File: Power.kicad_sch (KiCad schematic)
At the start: 76 parts, among them U1 TPS546D24ARVFR, U3 TPSM861253RDXR, U4 TPS546D24ARVFR, U5 L78L05_SOT89

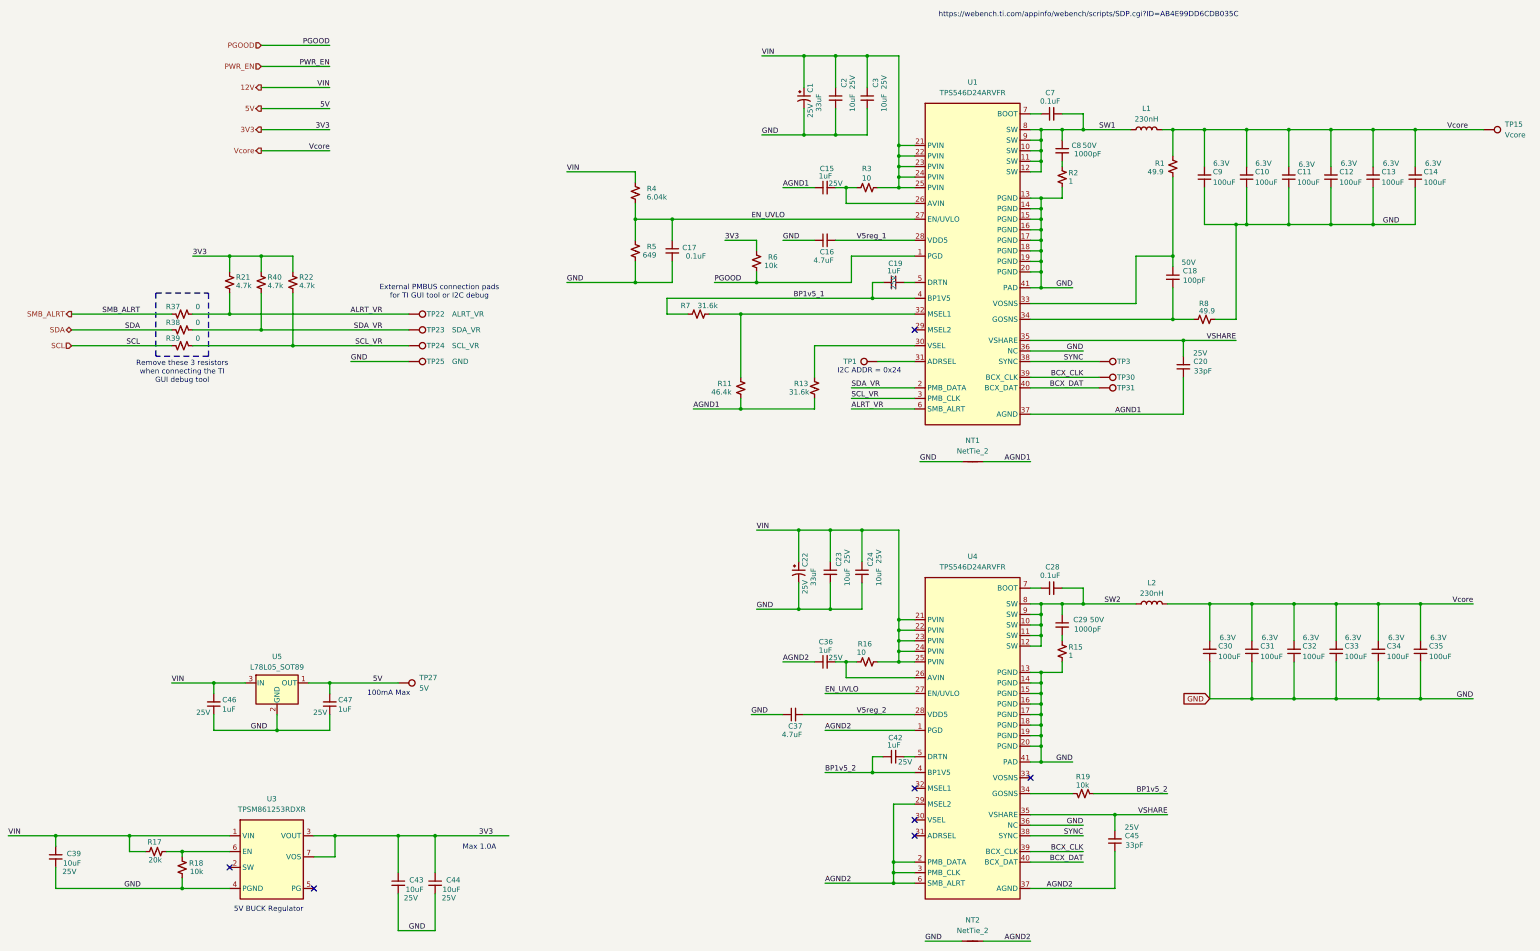
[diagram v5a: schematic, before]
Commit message: switched to single phase TPS546D24 and put the ASICs in series.
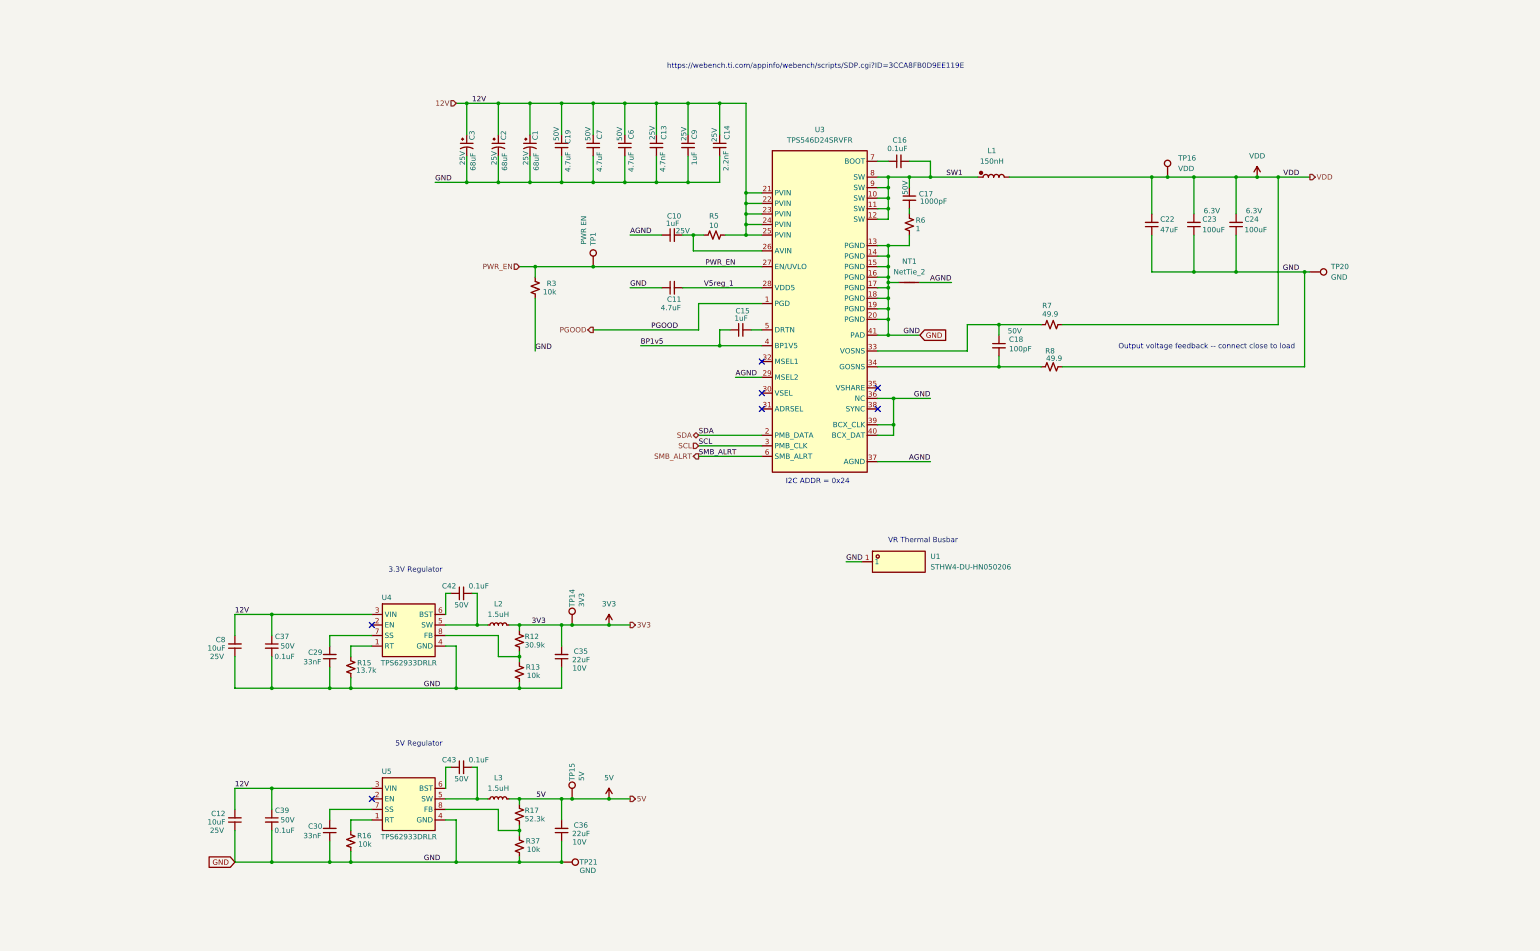
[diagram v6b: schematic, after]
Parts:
- removed C2, C3, C44: 10uF, Capacitor_SMD:C_0603_1608Metric, symbol Device:C_Small
- removed C20, C45: 33pF, Capacitor_SMD:C_0402_1005Metric, symbol Device:C_Small
- removed C22: 33uF, Capacitor_Tantalum_SMD:CP_EIA-7343-31_Kemet-D, symbol Device:C_Polarized_Small_US
- removed C28: 0.1uF, Capacitor_SMD:C_0402_1005Metric, symbol Device:C_Small
- removed C31, C32, C33, C34: 100uF, Capacitor_SMD:C_1206_3216Metric, symbol Device:C_Small
- removed C46, C47: 1uF, Capacitor_SMD:C_0402_1005Metric, symbol Device:C_Small
- removed L1, L2: 230nH, bitaxe:FP1107R1, symbol Device:L
- removed NT1, NT2: NetTie_2, bitaxe:NetTie-2_SMD_Pad0.2mmx1mm, symbol Device:NetTie_2
- removed R1: 49.9, Resistor_SMD:R_0402_1005Metric, symbol Device:R_Small_US
- removed R11: 46.4k, Resistor_SMD:R_0402_1005Metric, symbol Device:R_Small_US
- removed R18, R19: 10k, Resistor_SMD:R_0402_1005Metric, symbol Device:R_Small_US
- removed R2: 1, Resistor_SMD:R_0805_2012Metric, symbol Device:R_Small_US
- removed R21, R22, R40: 4.7k, Resistor_SMD:R_0402_1005Metric, symbol Device:R_Small_US
- removed R38, R39: 0, Resistor_SMD:R_0402_1005Metric, symbol Device:R_Small_US
- removed R4: 6.04k, Resistor_SMD:R_0402_1005Metric, symbol Device:R_Small_US
- removed TP22: ALRT_VR, TestPoint:TestPoint_Pad_D1.0mm, symbol Connector:TestPoint
- removed TP23: SDA_VR, TestPoint:TestPoint_Pad_D1.0mm, symbol Connector:TestPoint
- removed TP24: SCL_VR, TestPoint:TestPoint_Pad_D1.0mm, symbol Connector:TestPoint
- removed TP25: GND, TestPoint:TestPoint_Pad_D1.0mm, symbol Connector:TestPoint
- removed TP27: 5V, TestPoint:TestPoint_Pad_D1.5mm, symbol Connector:TestPoint
- removed TP3, TP30: BCX_CLK, TestPoint:TestPoint_Pad_D1.0mm, symbol Connector:TestPoint
- removed TP31: BCX_DAT, TestPoint:TestPoint_Pad_D1.0mm, symbol Connector:TestPoint
- removed U1, U4: TPS546D24ARVFR, bitaxe:LQFN40-CLIP, symbol bitaxe:TPS546D24
- removed U3: TPSM861253RDXR, bitaxe:TPSM863257RDX, symbol bitaxe:TPSM861253RDXR
- removed U5: L78L05_SOT89, Package_TO_SOT_SMD:SOT-89-3, symbol Regulator_Linear:L78L05_SOT89
- added C2, C3: 68uF, Capacitor_SMD:CP_Elec_5x5.8, symbol Device:C_Polarized_Small_US
- added C22: 47uF, Capacitor_SMD:C_0805_2012Metric, symbol Device:C_Small
- added C6: 4.7uF, Capacitor_SMD:C_1206_3216Metric, symbol Device:C_Small
- added L1: 150nH, symbol bitaxe:L-polarized
- added L2, L3: 1.5uH, bitaxe:IND-SMD_L2.0-W1.6, symbol Device:L_Small
- added NT1: NetTie_2, bitaxe:NetTie-2_SMD_Pad0.2mmx1mm, symbol bitaxe:NetTie_2
- added R12: 30.9k, Resistor_SMD:R_0402_1005Metric, symbol Device:R_Small_US
- added TP14: 3V3, bitaxe:TestPoint_Pad_D1.0mm, symbol Connector:TestPoint
- added TP16: VDD, bitaxe:TestPoint_Pad_D1.0mm, symbol Connector:TestPoint
- added TP20, TP21: GND, bitaxe:TestPoint_Pad_D1.0mm, symbol Connector:TestPoint
- added U1: STHW4-DU-HN050206, bitaxeProto:PAD-SMD_L5.0-W2.0_STHW4-DU-HN050206, symbol bitaxe:STHW4-DU-HN050206
- added U3: TPS546D24SRVFR, bitaxe:LQFN40-CLIP, symbol bitaxe:TPS546D24
- added U4, U5: TPS62933DRLR, bitaxe:SOT-583-8_L2.1-W1.2-P0.50-LS1.6-BR, symbol bitaxe:TPS62933DRLR
- C1: value 33uF -> 68uF; footprint Capacitor_Tantalum_SMD:CP_EIA-7343-31_Kemet-D -> Capacitor_SMD:CP_Elec_5x5.8; DK 399-3882-1-ND -> 493-16429-1-ND; PARTNO T495D336K025ATE300 -> UCM1E680MCL1GS
- C10, C9: value 100uF -> 1uF; footprint Capacitor_SMD:C_1206_3216Metric -> Capacitor_SMD:C_0603_1608Metric; DK 1276-1782-1-ND -> 1276-1184-1-ND; PARTNO CL31A107MQHNNNE -> CL10B105KA8NNNC; Voltage 6.3V -> 25V
- C11: value 100uF -> 4.7uF; footprint Capacitor_SMD:C_1206_3216Metric -> Capacitor_SMD:C_0402_1005Metric; DK 1276-1782-1-ND -> 490-14306-1-ND; PARTNO CL31A107MQHNNNE -> GRM155R61A475MEAAD; Voltage 6.3V -> (none)
- C12: value 100uF -> 10uF; footprint Capacitor_SMD:C_1206_3216Metric -> Capacitor_SMD:C_0603_1608Metric; DK 1276-1782-1-ND -> 490-18214-1-ND; LCSC (none) -> C15850; PARTNO CL31A107MQHNNNE -> GRM188R61E106KA73D; Voltage 6.3V -> 25V
- C13: value 100uF -> 4.7nF; footprint Capacitor_SMD:C_1206_3216Metric -> Capacitor_SMD:C_0402_1005Metric; DK 1276-1782-1-ND -> 490-1309-1-ND; PARTNO CL31A107MQHNNNE -> GRM155R71E472KA01D; Voltage 6.3V -> 25V
- C14: value 100uF -> 2.2nF; footprint Capacitor_SMD:C_1206_3216Metric -> Capacitor_SMD:C_0402_1005Metric; DK 1276-1782-1-ND -> 490-8257-1-ND; PARTNO CL31A107MQHNNNE -> GRM155R61H222KA01D; Voltage 6.3V -> 25V
- C15: DK 587-2984-1-ND -> 587-5514-1-ND; LCSC (none) -> C52923; PARTNO TMK107B7105KA-T -> EMK105BJ105MV-F; Voltage 25V -> (none)
- C16, C37: value 4.7uF -> 0.1uF; DK 490-14306-1-ND -> 490-10700-1-ND; LCSC (none) -> C77020; PARTNO GRM155R61A475MEAAD -> GRM155R71H104KE14D; Voltage (none) -> 50V
- C17: value 0.1uF -> 1000pF; footprint Capacitor_SMD:C_0402_1005Metric -> Capacitor_SMD:C_0805_2012Metric; DK 478-KGM05AR71C104KHCT-ND -> 311-1127-1-ND; PARTNO KGM05AR71C104KH -> CC0805KRX7R9BB102; Voltage (none) -> 50V
- C19: value 1uF -> 4.7uF; footprint Capacitor_SMD:C_0402_1005Metric -> Capacitor_SMD:C_1206_3216Metric; DK 587-2984-1-ND -> 490-6521-1-ND; PARTNO TMK107B7105KA-T -> GRM31CR71H475KA12L; Voltage 25V -> 50V
- C23, C24: value 10uF -> 100uF; footprint Capacitor_SMD:C_0603_1608Metric -> Capacitor_SMD:C_1210_3225Metric; DK 490-18214-1-ND -> 490-6533-1-ND; PARTNO GRM188R61E106KA73D -> GRM32EC80J107ME20L; Voltage 25V -> 6.3V
- C29: value 1000pF -> 33nF; footprint Capacitor_SMD:C_0805_2012Metric -> Capacitor_SMD:C_0402_1005Metric; DK 311-1127-1-ND -> 13-CC0402KRX7R9BB333CT-ND; LCSC (none) -> C106862; PARTNO CC0805KRX7R9BB102 -> CC0402KRX7R9BB333; Voltage 50V -> (none)
- C30: value 100uF -> 33nF; footprint Capacitor_SMD:C_1206_3216Metric -> Capacitor_SMD:C_0402_1005Metric; DK 1276-1782-1-ND -> 13-CC0402KRX7R9BB333CT-ND; LCSC (none) -> C106862; PARTNO CL31A107MQHNNNE -> CC0402KRX7R9BB333; Voltage 6.3V -> (none)
- C35: value 100uF -> 22uF; footprint Capacitor_SMD:C_1206_3216Metric -> Capacitor_SMD:C_0805_2012Metric; DK 1276-1782-1-ND -> 1276-2910-1-ND; LCSC (none) -> C45783; PARTNO CL31A107MQHNNNE -> CL21A226MPQNNNE; Voltage 6.3V -> 10V
- C36: value 1uF -> 22uF; footprint Capacitor_SMD:C_0402_1005Metric -> Capacitor_SMD:C_0805_2012Metric; DK 587-2984-1-ND -> 1276-2910-1-ND; LCSC (none) -> C45783; PARTNO TMK107B7105KA-T -> CL21A226MPQNNNE; Voltage 25V -> 10V
- C39: value 10uF -> 0.1uF; footprint Capacitor_SMD:C_0603_1608Metric -> Capacitor_SMD:C_0402_1005Metric; DK 490-18214-1-ND -> 490-10700-1-ND; LCSC (none) -> C77020; PARTNO GRM188R61E106KA73D -> GRM155R71H104KE14D; Voltage 25V -> 50V
- C42: value 1uF -> 0.1uF; DK 587-2984-1-ND -> 490-10700-1-ND; LCSC (none) -> C77020; Manufacturer (none) -> Murata Electronics; PARTNO TMK107B7105KA-T -> GRM155R71H104KE14D; Voltage 25V -> 50V
- C43: value 10uF -> 0.1uF; footprint Capacitor_SMD:C_0603_1608Metric -> Capacitor_SMD:C_0402_1005Metric; DK 490-18214-1-ND -> 490-10700-1-ND; LCSC (none) -> C77020; Manufacturer (none) -> Murata Electronics; PARTNO GRM188R61E106KA73D -> GRM155R71H104KE14D; Voltage 25V -> 50V
- C7: value 0.1uF -> 4.7uF; footprint Capacitor_SMD:C_0402_1005Metric -> Capacitor_SMD:C_1206_3216Metric; DK 478-KGM05AR71C104KHCT-ND -> 490-6521-1-ND; PARTNO KGM05AR71C104KH -> GRM31CR71H475KA12L; Voltage (none) -> 50V
- C8: value 1000pF -> 10uF; footprint Capacitor_SMD:C_0805_2012Metric -> Capacitor_SMD:C_0603_1608Metric; DK 311-1127-1-ND -> 490-18214-1-ND; LCSC (none) -> C15850; PARTNO CC0805KRX7R9BB102 -> GRM188R61E106KA73D; Voltage 50V -> 25V
- R13: value 31.6k -> 10k; DK YAG3115CT-ND -> 311-10KJRCT-ND; LCSC (none) -> C25744; PARTNO RC0402FR-0731K6L -> RC0402JR-0710KL
- R15: value 1 -> 13.7k; footprint Resistor_SMD:R_0805_2012Metric -> Resistor_SMD:R_0402_1005Metric; DK RHM1KTR-ND -> 311-13.7KLRCT-ND; LCSC (none) -> C274888; PARTNO ESR10EZPJ1R0 -> RC0402FR-0713K7L
- R16, R3: value 10 -> 10k; DK 311-10.0LRCT-ND -> 311-10KJRCT-ND; LCSC (none) -> C25744; PARTNO RC0402FR-0710RL -> RC0402JR-0710KL
- R17: value 20k -> 52.3k; DK 311-20.0KLRCT-ND -> YAG3179CT-ND; PARTNO RC0402FR-0720KL -> RC0402FR-0752K3L
- R37: value 0 -> 10k; DK 311-0.0JRCT-ND -> 311-10KJRCT-ND; LCSC (none) -> C25744; PARTNO RC0402JR-070RL -> RC0402JR-0710KL
- R5: value 649 -> 10; DK YAG3206CT-ND -> 311-10.0LRCT-ND; PARTNO RC0402FR-07649RL -> RC0402FR-0710RL
- R6: value 10k -> 1; footprint Resistor_SMD:R_0402_1005Metric -> Resistor_SMD:R_0805_2012Metric; DK 311-10KJRCT-ND -> RHM1KCT-ND; PARTNO RC0402JR-0710KL -> ESR10EZPJ1R0
- R7: value 31.6k -> 49.9; DK YAG3115CT-ND -> 311-49.9LRCT-ND; PARTNO RC0402FR-0731K6L -> RC0402FR-0749R9L
- TP1: value TestPoint -> PWR EN; footprint TestPoint:TestPoint_Pad_D1.0mm -> bitaxe:TestPoint_Pad_D1.0mm
- TP15: value Vcore -> 5V; footprint TestPoint:TestPoint_Pad_D1.5mm -> bitaxe:TestPoint_Pad_D1.0mm
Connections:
- net AGND2 is gone; now on net GND: C36.1
- net ALRT_VR is gone; now on an unnamed net: R37.2
- net SW2 is gone; now on net GND: C29.1
- net V5reg_2 is gone; now on net GND: C37.2
- net 12V: now also C12.2, C13.1, C14.1, C19.1, C37.1, C7.1, C8.2, C9.1, R5.1, C2.1, C3.1, C6.1, U3.21 (PVIN), U3.22 (PVIN), U3.23 (PVIN), U3.24 (PVIN), U3.25 (PVIN), U4.3 (VIN), U5.3 (VIN); no longer C23.1, C24.1, R16.1, R17.2, R3.1
- net 3V3: now also C35.2, L2.2, R12.2, TP14.1; no longer C43.1, R6.2
- net 5V: now also C36.2, R17.2, TP15.1, L3.2
- net GND: now also C13.2, C14.2, C19.2, C23.1, C24.1, C7.2, C8.1, C9.2, R13.1, R15.1, R16.1, R3.1, R37.1, R6.2, C2.2, C22.1, C3.2, C6.2, NT1.1, TP20.1, TP21.1, U1.1, U3.13 (PGND), U3.14 (PGND), U3.15 (PGND), U3.16 (PGND), U3.17 (PGND), U3.18 (PGND), U3.19 (PGND), U3.20 (PGND), U3.36 (NC), U3.39 (BCX_CLK), U3.40 (BCX_DAT), U3.41 (PAD), U4.4 (GND), U5.4 (GND); no longer C10.1, C13.1, C14.1, C16.1, C17.2, C23.2, C24.2, C37.1, C43.2, C9.1, R15.2, R5.1
- net PGOOD: now also U3.1 (PGD); no longer R6.1
- net PWR_EN: now also R3.2, TP1.1, U3.27 (EN/UVLO)
- net SCL: now also U3.3 (PMB_CLK)
- net SDA: now also U3.2 (PMB_DATA)
- net SMB_ALRT: now also U3.6 (SMB_ALRT); no longer R37.1
- net SW1: now also C16.2, C17.1, L1.1, U3.10 (SW), U3.11 (SW), U3.12 (SW), U3.8 (SW), U3.9 (SW); no longer C7.2, C8.1
- net V5reg_1: now also C11.2, U3.28 (VDD5); no longer C16.2
- net at C18.2, R8.1: now also U3.34 (GOSNS)
- net VDD: now reaches R7.1
- net VDD: now also C23.2, C24.2, C22.2, L1.2, TP16.1
- net at R17.1: now also U5.8 (FB)
- net at C18.1: now also R7.2, U3.33 (VOSNS)
- net at C29.2: now also U4.7 (SS); no longer R15.1
- net at C15.2: now also U3.5 (DRTN); no longer R3.2
- net at R13.2: now also R12.1, U4.8 (FB)
- net at R16.2: now also U5.1 (RT); no longer C36.2
- net at C42.2: now also L2.1, U4.5 (SW)
- net AGND1 renamed BP1v5
- net BP1v5: now also U3.4 (BP1V5); no longer R13.1
- removed net BP1v5_1: C19.1, R7.2
- net BP1v5_2: no longer names the net of C42.1
- net BP1v5_2: now also U4.6 (BST)
- net EN_UVLO: no longer names the net of R5.2
- net EN_UVLO: now also C10.2, U3.26 (AVIN); no longer C17.1
- removed net Vcore: C10.2, C11.2, C12.2, C13.2, C14.2, C30.2, C35.2, C9.2, TP15.1
- new net: C17.2, R6.1
- new net: C16.1, U3.7 (BOOT)
- new net: R15.2, U4.1 (RT)
- new net: C43.1, U5.6 (BST)
- new net: C43.2, L3.1, U5.5 (SW)
- new net: C30.2, U5.7 (SS)
- new net AGND: C10.1, NT1.2, U3.29 (MSEL2), U3.37 (AGND)
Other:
- note added: "3.3V Regulator"
- note added: "5V Regulator"
- note added: "Output voltage feedback -- connect close to load"
- note added: "VR Thermal Busbar"
- note added: "https://webench.ti.com/appinfo/webench/scripts/SDP.cgi?ID=3CCA8FB0D9EE119E"
- note removed: "100mA Max"
- note removed: "5V BUCK Regulator"
- note removed: "External PMBUS connection pads for TI GUI tool or I2C debug"
- note removed: "Max 1.0A"
- note removed: "Remove these 3 resistors when connecting the TI GUI debug tool"
- note removed: "https://webench.ti.com/appinfo/webench/scripts/SDP.cgi?ID=AB4E99DD6CDB035C"

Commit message: rough parts placement.
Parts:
- L1: footprint (none) -> bitaxe:GDIM107050-R15S1MTF-0R37
- U1: footprint bitaxeProto:PAD-SMD_L5.0-W2.0_STHW4-DU-HN050206 -> bitaxe:PAD-SMD_L5.0-W2.0_STHW4-DU-HN050206
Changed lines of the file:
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@@
 			)
 		)
-		(property "Footprint" "bitaxeProto:PAD-SMD_L5.0-W2.0_STHW4-DU-HN050206"
+		(property "Footprint" "bitaxe:PAD-SMD_L5.0-W2.0_STHW4-DU-HN050206"
 			(at 233.68 166.37 0)
 			(hide yes)
@@
 			)
 		)
-		(property "Footprint" ""
+		(property "Footprint" "bitaxe:GDIM107050-R15S1MTF-0R37"
 			(at 260.35 66.04 0)
 			(hide yes)

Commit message: finished routing
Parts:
- removed NT1: NetTie_2, bitaxe:NetTie-2_SMD_Pad0.2mmx1mm, symbol bitaxe:NetTie_2
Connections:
- net AGND is gone; now on net GND: C10.1, U3.29 (MSEL2), U3.37 (AGND)
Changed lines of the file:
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@@
 	)
 	(junction
-		(at 234.95 91.44)
-		(diameter 0)
-		(color 0 0 0 0)
-	)
-	(junction
 		(at 200.66 69.85)
 		(diameter 0)
@@
 	(wire
 		(pts
-			(xy 234.95 90.17) (xy 234.95 91.44)
-		)
-		(stroke
-			(width 0)
-			(type default)
-		)
-	)
-	(wire
-		(pts
 			(xy 135.89 215.9) (xy 138.43 215.9)
 		)
@@
 	(wire
 		(pts
-			(xy 234.95 91.44) (xy 234.95 92.71)
+			(xy 234.95 90.17) (xy 234.95 92.71)
 		)
 		(stroke
@@
 	(wire
 		(pts
-			(xy 234.95 97.79) (xy 234.95 100.33)
-		)
-		(stroke
-			(width 0)
-			(type default)
-		)
-	)
-	(wire
-		(pts
 			(xy 204.47 96.52) (xy 189.23 96.52)
 		)
@@
 	(wire
 		(pts
+			(xy 234.95 95.25) (xy 234.95 100.33)
+		)
+		(stroke
+			(width 0)
+			(type default)
+		)
+	)
+	(wire
+		(pts
 			(xy 163.83 87.63) (xy 204.47 87.63)
 		)
@@
 	(wire
 		(pts
-			(xy 234.95 95.25) (xy 234.95 97.79)
-		)
-		(stroke
-			(width 0)
-			(type default)
-		)
-	)
-	(wire
-		(pts
 			(xy 105.41 189.23) (xy 105.41 186.69)
 		)
@@
 	(wire
 		(pts
-			(xy 234.95 91.44) (xy 237.49 91.44)
-		)
-		(stroke
-			(width 0)
-			(type default)
-		)
-	)
-	(wire
-		(pts
 			(xy 156.21 189.23) (xy 146.05 189.23)
 		)
@@
 	(wire
 		(pts
-			(xy 242.57 91.44) (xy 250.19 91.44)
-		)
-		(stroke
-			(width 0)
-			(type default)
-		)
-	)
-	(wire
-		(pts
 			(xy 328.93 66.04) (xy 336.55 66.04)
 		)
@@
 		)
 	)
-	(label "AGND"
+	(label "GND"
 		(at 172.72 80.01 0)
 		(effects
@@
 		)
 	)
-	(label "AGND"
+	(label "GND"
 		(at 198.12 114.3 0)
 		(effects
@@
 		)
 	)
-	(label "AGND"
+	(label "GND"
 		(at 245.11 134.62 180)
 		(effects
@@
 		)
 	)
-	(label "AGND"
-		(at 250.19 91.44 180)
-		(effects
-			(font
-				(size 1.27 1.27)
-			)
-			(justify right bottom)
-		)
-	)
 	(global_label "GND"
 		(shape input)
@@
 					(unit 1)
 				)
-			)
-		)
-	)
-	(symbol
-		(lib_id "bitaxe:NetTie_2")
-		(at 240.03 91.44 0)
-		(unit 1)
-		(body_style 1)
-		(exclude_from_sim no)
-		(in_bom no)
-		(on_board yes)
-		(in_pos_files yes)
-		(dnp no)
-		(fields_autoplaced yes)
-		(property "Reference" "NT1"
-			(at 240.03 86.36 0)
-			(show_name no)
-			(do_not_autoplace no)
-			(effects
-				(font
-					(size 1.27 1.27)
-				)
-			)
-		)
-		(property "Value" "NetTie_2"
-			(at 240.03 88.9 0)
-			(show_name no)
-			(do_not_autoplace no)
-			(effects
-				(font
-					(size 1.27 1.27)
-				)
-			)
-		)
-		(property "Footprint" "bitaxe:NetTie-2_SMD_Pad0.2mmx1mm"
-			(at 240.03 91.44 0)
-			(hide yes)
-			(show_name no)
-			(do_not_autoplace no)
-			(effects
-				(font
-					(size 1.27 1.27)
-				)
-			)
-		)
-		(property "Datasheet" ""
-			(at 240.03 91.44 0)
-			(hide yes)
-			(show_name no)
-			(do_not_autoplace no)
-			(effects
-				(font
-					(size 1.27 1.27)
-				)
-			)
-		)
-		(property "Description" "Net tie, 2 pins"
-			(at 240.03 91.44 0)
-			(hide yes)
-			(show_name no)
-			(do_not_autoplace no)
-			(effects
-				(font
-					(size 1.27 1.27)
-				)
-			)
-		)
-		(property "Manufacturer" ""
-			(at 240.03 91.44 0)
-			(hide yes)
-			(show_name no)
-			(do_not_autoplace no)
-			(effects
-				(font
-					(size 1.27 1.27)
-				)
-			)
-		)
-		(property "Sim.Device" ""
-			(at 240.03 91.44 0)
-			(hide yes)
-			(show_name no)
-			(do_not_autoplace no)
-			(effects
-				(font
-					(size 1.27 1.27)
-				)
-			)
-		)
-		(property "Sim.Pins" ""
-			(at 240.03 91.44 0)
-			(hide yes)
-			(show_name no)
-			(do_not_autoplace no)
-			(effects
-				(font
-					(size 1.27 1.27)
-				)
-			)
-		)
-		(pin "2"
-		)
-		(pin "1"
-		)
-		(instances
-			(project "bitaxeNaja"
-				(path "/61fe8d2c-9301-4ad9-8caf-c47acfa835b0/24036843-8461-4d4b-b738-f953c909ed6c"
-					(reference "NT1")
-					(unit 1)
-				)
